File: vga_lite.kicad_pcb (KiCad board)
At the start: 6 copper layers, 45 x 85 mm, 71 parts, among them J1 JFAG, J2 Power, J3 CPU ADDR, J4 CPU DATA, J5 CPU Clock, J6 SPI, J7 VGA Out, U2 M95M02, U3 ICE40HX4K-TQ144, U4 AZ1117-3.3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

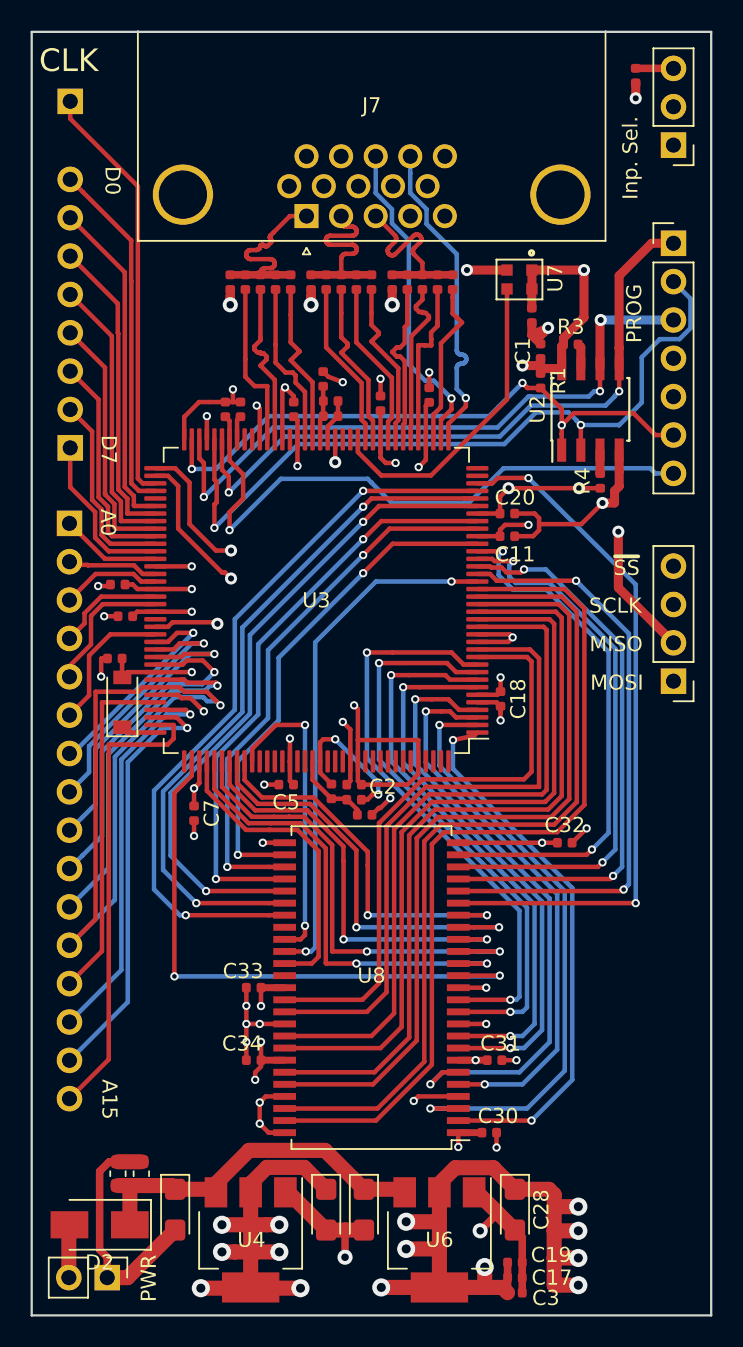
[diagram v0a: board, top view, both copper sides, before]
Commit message: Added PCB image
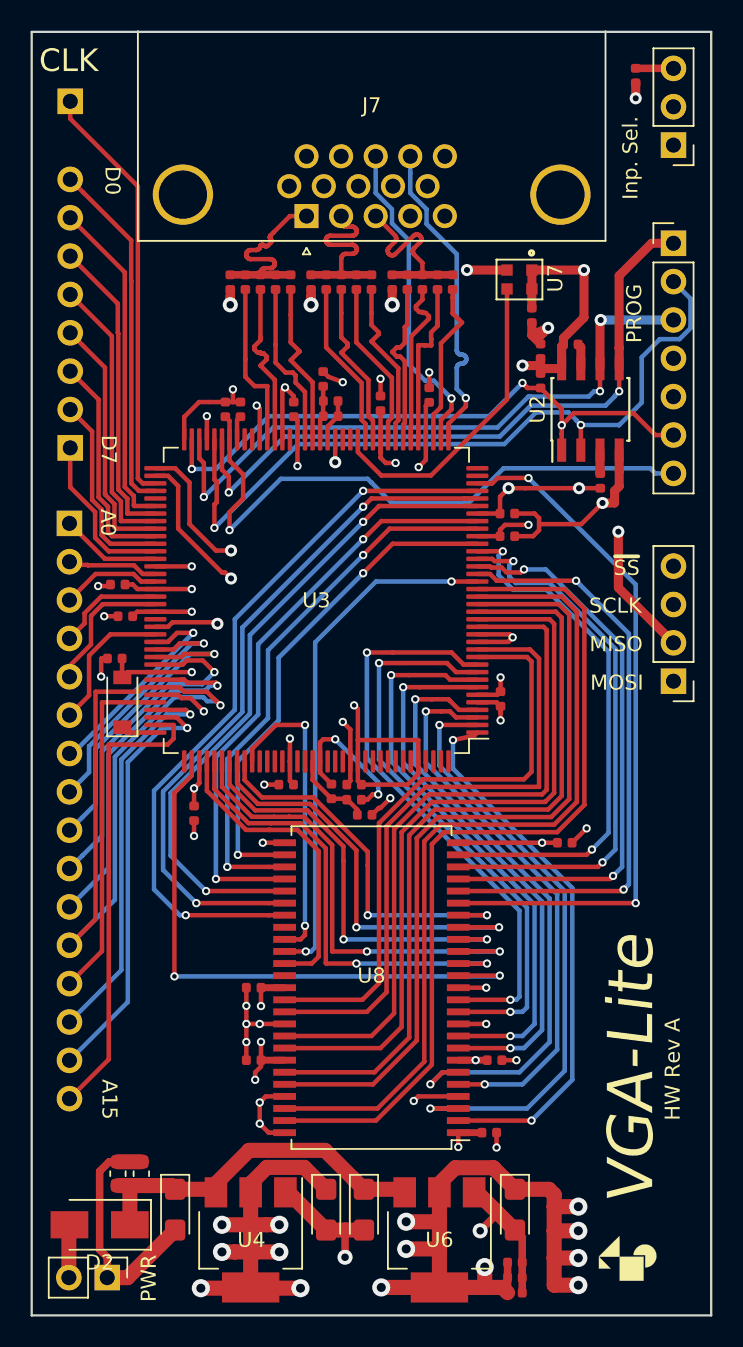
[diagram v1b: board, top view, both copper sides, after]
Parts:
- added G***: LOGO, MyLibs:merchant_small, F.Cu at (169.5, 126.2)
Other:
- board text added: "HW Rev A"
- board text added: "VGA-Lite"
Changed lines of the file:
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@@
   (general
     (thickness 1.6)
-    (drawings 24)
+    (drawings 26)
     (tracks 1563)
     (zones 0)
-    (modules 71)
+    (modules 72)
     (nets 141)
   )
@@
     (tags capacitor)
     (attr smd)
-    (fp_text reference C1 (at 0 -1.17 90) (layer F.SilkS)
+    (fp_text reference C1 (at 0 -1.17 90) (layer F.Fab)
       (effects (font (size 1 1) (thickness 0.15)))
     )
@@
     (tags capacitor)
     (attr smd)
-    (fp_text reference C2 (at 1.9 0.15) (layer F.SilkS)
+    (fp_text reference C2 (at 1.9 0.15) (layer F.Fab)
       (effects (font (size 1 1) (thickness 0.15)))
     )
@@
     (tags capacitor)
     (attr smd)
-    (fp_text reference C3 (at 2.05 0.35) (layer F.SilkS)
+    (fp_text reference C3 (at 2.05 0.35) (layer F.Fab)
       (effects (font (size 1 1) (thickness 0.15)))
     )
@@
     (tags capacitor)
     (attr smd)
-    (fp_text reference C5 (at 0 -1.17 180) (layer F.SilkS)
+    (fp_text reference C5 (at 0 -1.17 180) (layer F.Fab)
       (effects (font (size 1 1) (thickness 0.15)))
     )
@@
     (tags capacitor)
     (attr smd)
-    (fp_text reference C7 (at 0 -1.17 270) (layer F.SilkS)
+    (fp_text reference C7 (at 0 -1.17 270) (layer F.Fab)
       (effects (font (size 1 1) (thickness 0.15)))
     )
@@
     (tags capacitor)
     (attr smd)
-    (fp_text reference C11 (at 0.504949 1.202082) (layer F.SilkS)
+    (fp_text reference C11 (at 0.504949 1.202082) (layer F.Fab)
       (effects (font (size 1 1) (thickness 0.15)))
     )
@@
     (tags capacitor)
     (attr smd)
-    (fp_text reference C17 (at 2.45 0) (layer F.SilkS)
+    (fp_text reference C17 (at 2.45 0) (layer F.Fab)
       (effects (font (size 1 1) (thickness 0.15)))
     )
@@
     (tags capacitor)
     (attr smd)
-    (fp_text reference C18 (at 0 -1.17 270) (layer F.SilkS)
+    (fp_text reference C18 (at 0 -1.17 270) (layer F.Fab)
       (effects (font (size 1 1) (thickness 0.15)))
     )
@@
     (tags capacitor)
     (attr smd)
-    (fp_text reference C19 (at 2.4 -0.5) (layer F.SilkS)
+    (fp_text reference C19 (at 2.4 -0.5) (layer F.Fab)
       (effects (font (size 1 1) (thickness 0.15)))
     )
@@
     (tags capacitor)
     (attr smd)
-    (fp_text reference C20 (at 0.504949 -1.06066) (layer F.SilkS)
+    (fp_text reference C20 (at 0.504949 -1.06066) (layer F.Fab)
       (effects (font (size 1 1) (thickness 0.15)))
     )
@@
     (tags "capacitor tantalum")
     (attr smd)
-    (fp_text reference C28 (at 0 -1.75 270) (layer F.SilkS)
+    (fp_text reference C28 (at 0 -1.75 270) (layer F.Fab)
       (effects (font (size 1 1) (thickness 0.15)))
     )
@@
     (tags capacitor)
     (attr smd)
-    (fp_text reference C30 (at 0.585 -1.1) (layer F.SilkS)
+    (fp_text reference C30 (at 0.585 -1.1) (layer F.Fab)
       (effects (font (size 1 1) (thickness 0.15)))
     )
@@
     (tags capacitor)
     (attr smd)
-    (fp_text reference C31 (at 0.4 -1.1) (layer F.SilkS)
+    (fp_text reference C31 (at 0.4 -1.1) (layer F.Fab)
       (effects (font (size 1 1) (thickness 0.15)))
     )
@@
     (tags capacitor)
     (attr smd)
-    (fp_text reference C32 (at 0 -1.17) (layer F.SilkS)
+    (fp_text reference C32 (at 0 -1.17) (layer F.Fab)
       (effects (font (size 1 1) (thickness 0.15)))
     )
@@
     (tags capacitor)
     (attr smd)
-    (fp_text reference C33 (at 0.7 1.1 180) (layer F.SilkS)
+    (fp_text reference C33 (at 0.7 1.1 180) (layer F.Fab)
       (effects (font (size 1 1) (thickness 0.15)))
     )
@@
     (tags capacitor)
     (attr smd)
-    (fp_text reference C34 (at 0.75 1.1 180) (layer F.SilkS)
+    (fp_text reference C34 (at 0.75 1.1 180) (layer F.Fab)
       (effects (font (size 1 1) (thickness 0.15)))
     )
@@
     (tags resistor)
     (attr smd)
-    (fp_text reference R1 (at 0 -1.17 270) (layer F.SilkS)
+    (fp_text reference R1 (at 0 -1.17 270) (layer F.Fab)
       (effects (font (size 1 1) (thickness 0.15)))
     )
@@
     (tags resistor)
     (attr smd)
-    (fp_text reference R3 (at 0 -1.17) (layer F.SilkS)
+    (fp_text reference R3 (at 0 -1.17) (layer F.Fab)
       (effects (font (size 1 1) (thickness 0.15)))
     )
@@
     (tags resistor)
     (attr smd)
-    (fp_text reference R4 (at 0 -1.17 90) (layer F.SilkS)
+    (fp_text reference R4 (at 0 -1.17 90) (layer F.Fab)
       (effects (font (size 1 1) (thickness 0.15)))
     )
@@
       (net 2 +3V3))
   )
+  (module MyLibs:merchant_small (layer F.Cu)
+    (at 169.5 126.2 90)
+    (fp_text reference G*** (at 0 0 90) (layer F.SilkS) hide
+      (effects (font (size 1.524 1.524) (thickness 0.3)))
+    )
+    (fp_text value LOGO (at 0.75 0 90) (layer F.SilkS) hide
+      (effects (font (size 1.524 1.524) (thickness 0.3)))
+    )
+    (fp_poly (pts (xy 0.084667 -1.248834) (xy 0.084608 -1.354618) (xy 0.084436 -1.455377) (xy 0.08416 -1.549845)
+      (xy 0.083791 -1.636761) (xy 0.083335 -1.714859) (xy 0.082804 -1.782879) (xy 0.082205 -1.839554)
+      (xy 0.081548 -1.883624) (xy 0.080842 -1.913823) (xy 0.080096 -1.928889) (xy 0.079769 -1.9304)
+      (xy 0.073094 -1.92457) (xy 0.05548 -1.907747) (xy 0.027942 -1.880932) (xy -0.008508 -1.845129)
+      (xy -0.052855 -1.801338) (xy -0.104084 -1.750561) (xy -0.161184 -1.693801) (xy -0.223138 -1.632059)
+      (xy -0.288934 -1.566337) (xy -0.310097 -1.545167) (xy -0.376858 -1.478418) (xy -0.440065 -1.415335)
+      (xy -0.498707 -1.356919) (xy -0.551774 -1.304172) (xy -0.598255 -1.258096) (xy -0.637139 -1.21969)
+      (xy -0.667415 -1.189958) (xy -0.688073 -1.1699) (xy -0.698103 -1.160518) (xy -0.698899 -1.159934)
+      (xy -0.69968 -1.168122) (xy -0.700408 -1.191572) (xy -0.701066 -1.228613) (xy -0.701638 -1.277573)
+      (xy -0.702107 -1.336782) (xy -0.702456 -1.404567) (xy -0.70267 -1.479258) (xy -0.702733 -1.5494)
+      (xy -0.702733 -1.938867) (xy 0.097407 -1.938867) (xy 0.776837 -1.259398) (xy 0.865996 -1.170179)
+      (xy 0.951738 -1.084272) (xy 1.033309 -1.002439) (xy 1.109957 -0.92544) (xy 1.180927 -0.854035)
+      (xy 1.245465 -0.788985) (xy 1.302819 -0.73105) (xy 1.352235 -0.680991) (xy 1.392959 -0.63957)
+      (xy 1.424238 -0.607545) (xy 1.445319 -0.585678) (xy 1.455447 -0.57473) (xy 1.456267 -0.573598)
+      (xy 1.44801 -0.572618) (xy 1.42408 -0.571685) (xy 1.385735 -0.57081) (xy 1.334235 -0.570004)
+      (xy 1.27084 -0.56928) (xy 1.196809 -0.568648) (xy 1.113401 -0.568121) (xy 1.021876 -0.56771)
+      (xy 0.923494 -0.567427) (xy 0.819514 -0.567283) (xy 0.770467 -0.567267) (xy 0.084667 -0.567267)
+      (xy 0.084667 -1.248834)) (layer F.SilkS) (width 0.01))
+    (fp_poly (pts (xy 0.084667 1.024466) (xy -1.507066 1.024466) (xy -1.507066 -0.567267) (xy 0.084667 -0.567267)
+      (xy 0.084667 1.024466)) (layer F.SilkS) (width 0.01))
+    (fp_poly (pts (xy 0.240898 0.350109) (xy 0.280074 0.358164) (xy 0.325599 0.369985) (xy 0.372805 0.384262)
+      (xy 0.417026 0.399683) (xy 0.452967 0.414641) (xy 0.554986 0.47132) (xy 0.644796 0.539687)
+      (xy 0.722176 0.61947) (xy 0.786904 0.710394) (xy 0.838757 0.812187) (xy 0.877514 0.924577)
+      (xy 0.882196 0.942377) (xy 0.889272 0.973069) (xy 0.893857 1.001512) (xy 0.896252 1.032183)
+      (xy 0.896762 1.069561) (xy 0.895689 1.118124) (xy 0.895158 1.133999) (xy 0.89097 1.207766)
+      (xy 0.883307 1.26975) (xy 0.870983 1.324946) (xy 0.852811 1.378348) (xy 0.827606 1.434951)
+      (xy 0.82006 1.450199) (xy 0.762798 1.545585) (xy 0.692374 1.631461) (xy 0.610446 1.706509)
+      (xy 0.518674 1.76941) (xy 0.418716 1.818846) (xy 0.312993 1.85331) (xy 0.265337 1.86193)
+      (xy 0.207053 1.867737) (xy 0.143876 1.870579) (xy 0.081541 1.8703) (xy 0.025784 1.866748)
+      (xy -0.007885 1.861918) (xy -0.11233 1.8332) (xy -0.212579 1.78956) (xy -0.306018 1.732585)
+      (xy -0.390033 1.663861) (xy -0.460031 1.587499) (xy -0.480505 1.561546) (xy -0.497584 1.539957)
+      (xy -0.507954 1.526922) (xy -0.508658 1.526047) (xy -0.515815 1.514217) (xy -0.528198 1.490883)
+      (xy -0.543822 1.459864) (xy -0.554891 1.437147) (xy -0.575964 1.386965) (xy -0.595038 1.329827)
+      (xy -0.610729 1.271021) (xy -0.621654 1.215834) (xy -0.626431 1.169554) (xy -0.626533 1.163234)
+      (xy -0.626533 1.134533) (xy 0.194734 1.134533) (xy 0.194734 0.347133) (xy 0.212736 0.347133)
+      (xy 0.240898 0.350109)) (layer F.SilkS) (width 0.01))
+  )
+  (gr_text "HW Rev A" (at 172.45 113.7 90) (layer F.SilkS)
+    (effects (font (size 1 1) (thickness 0.25)))
+  )
+  (gr_text VGA-Lite (at 169.7 113.7 90) (layer F.SilkS)
+    (effects (font (size 3 3) (thickness 0.75) italic))
+  )
   (gr_text "Inp. Sel." (at 169.65 53.35 90) (layer F.SilkS)
